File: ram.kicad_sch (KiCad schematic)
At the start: 20 parts, among them U19 7130, U7 74HCT245

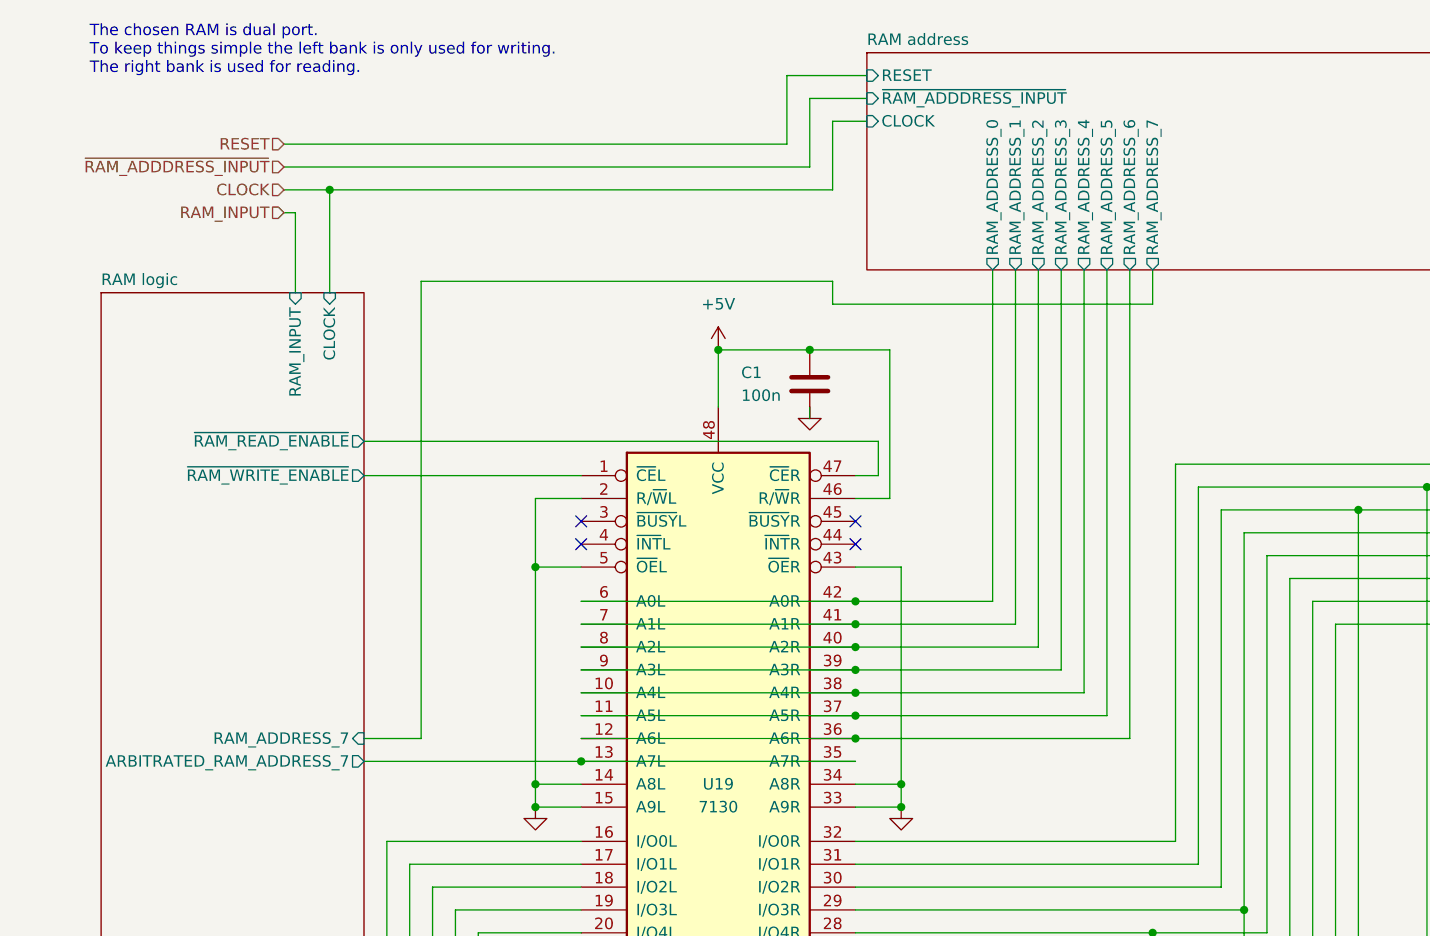
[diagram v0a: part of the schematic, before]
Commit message: ram address 7 led now uses the arbitrated signal
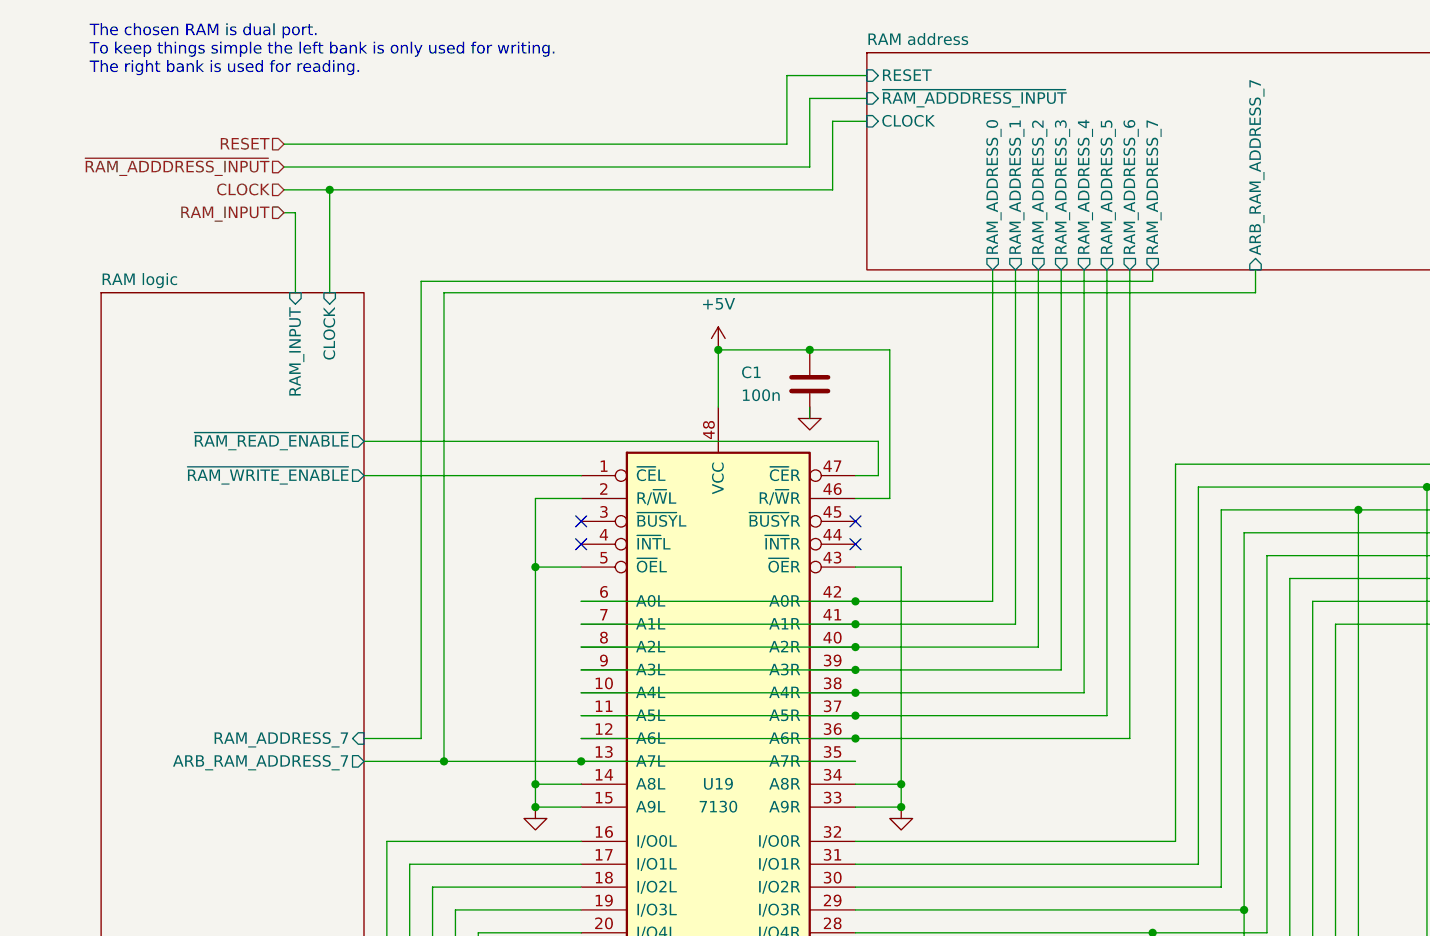
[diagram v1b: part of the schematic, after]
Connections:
- net RAM logic/ARBITRATED_RAM_ADDRESS_7 renamed RAM address/ARB_RAM_ADDRESS_7
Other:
- sheet RAM address ports: added ARB_RAM_ADDRESS_7; removed none
- sheet RAM logic ports: added ARB_RAM_ADDRESS_7; removed ARBITRATED_RAM_ADDRESS_7
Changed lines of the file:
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@@
   (junction (at 63.5 73.66) (diameter 0) (color 0 0 0 0)
+  )
+  (junction (at 53.34 95.25) (diameter 0) (color 0 0 0 0)
   )
   (junction (at 99.06 85.09) (diameter 0) (color 0 0 0 0)
@@
     (stroke (width 0) (type default))
   )
-  (wire (pts (xy 96.52 41.91) (xy 50.8 41.91))
+  (wire (pts (xy 50.8 41.91) (xy 132.08 41.91))
     (stroke (width 0) (type default))
   )
@@
     (stroke (width 0) (type default) (color 0 0 255 1))
   )
-  (wire (pts (xy 44.45 95.25) (xy 68.58 95.25))
-    (stroke (width 0) (type default))
-  )
-  (wire (pts (xy 132.08 44.45) (xy 96.52 44.45))
+  (wire (pts (xy 44.45 95.25) (xy 53.34 95.25))
     (stroke (width 0) (type default))
   )
@@
     (stroke (width 0) (type default))
   )
-  (wire (pts (xy 132.08 40.64) (xy 132.08 44.45))
+  (wire (pts (xy 132.08 40.64) (xy 132.08 41.91))
     (stroke (width 0) (type default))
   )
@@
     (stroke (width 0) (type default) (color 0 0 255 1))
   )
+  (wire (pts (xy 143.51 40.64) (xy 143.51 43.18))
+    (stroke (width 0) (type default))
+  )
   (wire (pts (xy 134.62 104.14) (xy 134.62 62.23))
     (stroke (width 0) (type default))
@@
     (stroke (width 0) (type default))
   )
+  (wire (pts (xy 53.34 95.25) (xy 68.58 95.25))
+    (stroke (width 0) (type default))
+  )
   (wire (pts (xy 99.06 119.38) (xy 111.76 119.38))
     (stroke (width 0) (type default))
@@
     (stroke (width 0) (type default) (color 255 0 0 1))
   )
+  (wire (pts (xy 143.51 43.18) (xy 53.34 43.18))
+    (stroke (width 0) (type default))
+  )
   (wire (pts (xy 256.54 31.75) (xy 256.54 74.93))
     (stroke (width 0) (type default) (color 0 0 255 1))
@@
     (stroke (width 0) (type default) (color 255 0 0 1))
   )
+  (wire (pts (xy 53.34 43.18) (xy 53.34 95.25))
+    (stroke (width 0) (type default))
+  )
   (wire (pts (xy 116.84 80.01) (xy 116.84 40.64))
     (stroke (width 0) (type default))
@@
   )
   (wire (pts (xy 147.32 116.84) (xy 121.92 116.84))
-    (stroke (width 0) (type default))
-  )
-  (wire (pts (xy 96.52 44.45) (xy 96.52 41.91))
     (stroke (width 0) (type default))
   )
@@
       (effects (font (size 1.27 1.27)) (justify left))
     )
+    (pin "ARB_RAM_ADDRESS_7" input (at 143.51 40.64 270)
+      (effects (font (size 1.27 1.27)) (justify left))
+    )
     (instances
       (project "8-bit-cpu"
@@
       (effects (font (size 1.27 1.27)) (justify left))
     )
-    (pin "ARBITRATED_RAM_ADDRESS_7" output (at 44.45 95.25 0)
-      (effects (font (size 1.27 1.27)) (justify right))
-    )
+    (pin "ARB_RAM_ADDRESS_7" output (at 44.45 95.25 0)
+      (effects (font (size 1.27 1.27)) (justify right))
+    )

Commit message: finished the control logic
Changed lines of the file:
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@@
     (effects (font (size 1.27 1.27)) (justify left))
   )
-  (hierarchical_label "~{RAM_OUTPUT}" (shape output) (at 269.24 100.33 0) (fields_autoplaced)
+  (hierarchical_label "~{RAM_OUTPUT}" (shape input) (at 269.24 100.33 0) (fields_autoplaced)
     (effects (font (size 1.27 1.27)) (justify left))
   )

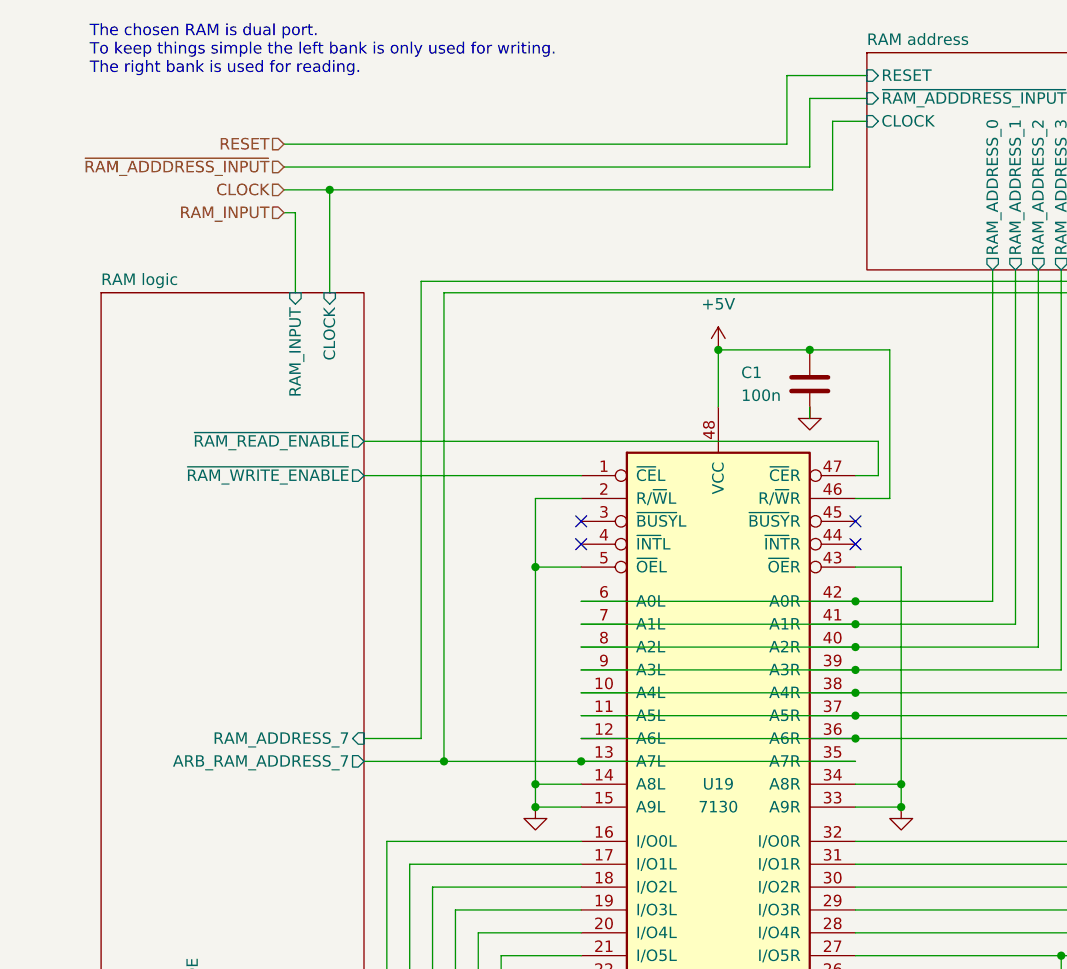
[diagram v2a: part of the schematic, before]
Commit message: added stack and x register.  Added logic for stack_address so ram address 7 gets passes and ram address 8 is high
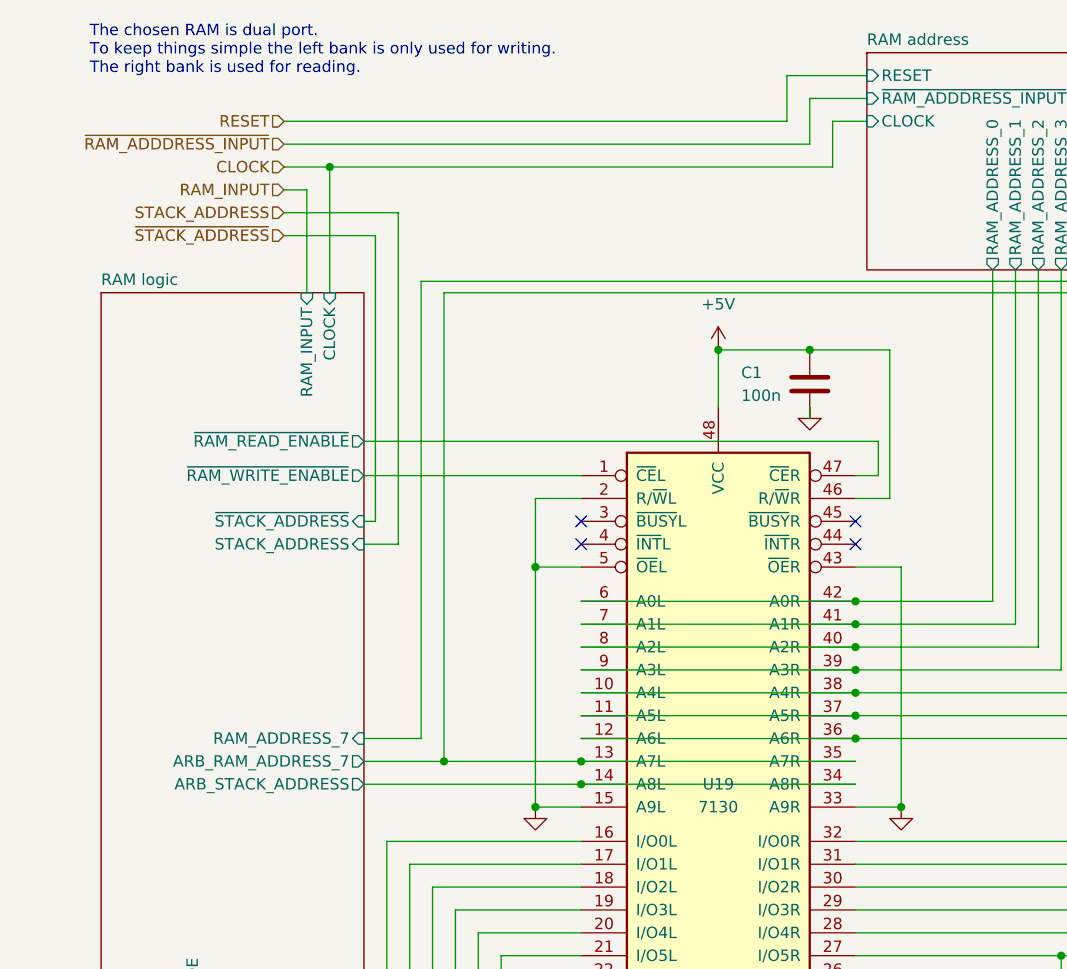
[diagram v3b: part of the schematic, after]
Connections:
- net GND: no longer U19.14 (A8L), U19.34 (A8R)
- new net RAM logic/ARB_STACK_ADDRESS: U19.14 (A8L), U19.34 (A8R)
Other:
- sheet RAM logic ports: added ARB_STACK_ADDRESS, STACK_ADDRESS, ~{STACK_ADDRESS}; removed none
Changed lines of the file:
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@@
   (junction (at 142.24 111.76) (diameter 0) (color 0 0 0 0)
   )
-  (junction (at 63.5 97.79) (diameter 0) (color 0 0 0 0)
-  )
   (junction (at 99.06 82.55) (diameter 0) (color 0 0 0 0)
   )
@@
   (junction (at 121.92 146.05) (diameter 0) (color 0 0 0 0)
   )
+  (junction (at 40.64 29.21) (diameter 0) (color 255 0 0 1)
+  )
   (junction (at 111.76 146.05) (diameter 0) (color 0 0 0 0)
   )
@@
   (junction (at 245.11 77.47) (diameter 0) (color 0 0 255 1)
   )
+  (junction (at 68.58 97.79) (diameter 0) (color 255 0 0 1)
+  )
   (junction (at 269.24 62.23) (diameter 0) (color 0 0 255 1)
   )
@@
   (junction (at 132.08 114.3) (diameter 0) (color 0 0 0 0)
   )
-  (junction (at 104.14 97.79) (diameter 0) (color 0 0 0 0)
-  )
   (junction (at 237.49 69.85) (diameter 0) (color 0 0 255 1)
   )
@@
   )
   (junction (at 142.24 146.05) (diameter 0) (color 0 0 0 0)
-  )
-  (junction (at 40.64 31.75) (diameter 0) (color 255 0 0 1)
   )
   (junction (at 132.08 146.05) (diameter 0) (color 0 0 0 0)
@@
     (stroke (width 0) (type default))
   )
-  (wire (pts (xy 91.44 26.67) (xy 35.56 26.67))
-    (stroke (width 0) (type default) (color 255 0 0 1))
-  )
-  (wire (pts (xy 99.06 97.79) (xy 104.14 97.79))
-    (stroke (width 0) (type default))
+  (wire (pts (xy 48.26 34.29) (xy 48.26 71.12))
+    (stroke (width 0) (type default) (color 255 0 0 1))
+  )
+  (wire (pts (xy 91.44 24.13) (xy 35.56 24.13))
+    (stroke (width 0) (type default) (color 255 0 0 1))
   )
   (wire (pts (xy 152.4 146.05) (xy 152.4 143.51))
     (stroke (width 0) (type default))
   )
-  (wire (pts (xy 93.98 29.21) (xy 35.56 29.21))
+  (wire (pts (xy 93.98 26.67) (xy 35.56 26.67))
     (stroke (width 0) (type default) (color 255 0 0 1))
   )
@@
     (stroke (width 0) (type default))
   )
+  (wire (pts (xy 35.56 36.83) (xy 45.72 36.83))
+    (stroke (width 0) (type default) (color 255 0 0 1))
+  )
   (wire (pts (xy 101.6 121.92) (xy 99.06 121.92))
     (stroke (width 0) (type default))
@@
     (stroke (width 0) (type default) (color 255 0 0 1))
   )
-  (wire (pts (xy 35.56 31.75) (xy 40.64 31.75))
+  (wire (pts (xy 35.56 29.21) (xy 40.64 29.21))
     (stroke (width 0) (type default) (color 255 0 0 1))
   )
@@
     (stroke (width 0) (type default) (color 0 0 255 1))
   )
-  (wire (pts (xy 36.83 34.29) (xy 36.83 43.18))
+  (wire (pts (xy 38.1 31.75) (xy 38.1 43.18))
     (stroke (width 0) (type default) (color 255 0 0 1))
   )
@@
     (stroke (width 0) (type default))
   )
-  (wire (pts (xy 104.14 73.66) (xy 104.14 97.79))
+  (wire (pts (xy 104.14 73.66) (xy 104.14 100.33))
     (stroke (width 0) (type default))
   )
@@
     (stroke (width 0) (type default))
   )
+  (wire (pts (xy 68.58 97.79) (xy 99.06 97.79))
+    (stroke (width 0) (type default) (color 255 0 0 1))
+  )
   (wire (pts (xy 198.12 29.21) (xy 259.08 29.21))
     (stroke (width 0) (type default) (color 0 0 255 1))
@@
     (stroke (width 0) (type default))
   )
-  (wire (pts (xy 104.14 97.79) (xy 104.14 100.33))
-    (stroke (width 0) (type default))
-  )
   (wire (pts (xy 149.86 119.38) (xy 149.86 77.47))
     (stroke (width 0) (type default))
@@
     (stroke (width 0) (type default))
   )
+  (wire (pts (xy 35.56 34.29) (xy 48.26 34.29))
+    (stroke (width 0) (type default) (color 255 0 0 1))
+  )
   (wire (pts (xy 68.58 92.71) (xy 99.06 92.71))
     (stroke (width 0) (type default))
@@
     (stroke (width 0) (type default))
   )
-  (wire (pts (xy 68.58 97.79) (xy 63.5 97.79))
-    (stroke (width 0) (type default))
-  )
   (wire (pts (xy 54.61 111.76) (xy 54.61 154.94))
     (stroke (width 0) (type default))
@@
     (stroke (width 0) (type default) (color 0 0 255 1))
   )
-  (wire (pts (xy 91.44 19.05) (xy 91.44 26.67))
+  (wire (pts (xy 91.44 19.05) (xy 91.44 24.13))
     (stroke (width 0) (type default) (color 255 0 0 1))
   )
@@
     (stroke (width 0) (type default))
   )
+  (wire (pts (xy 40.64 29.21) (xy 40.64 43.18))
+    (stroke (width 0) (type default) (color 255 0 0 1))
+  )
   (wire (pts (xy 59.69 116.84) (xy 59.69 154.94))
     (stroke (width 0) (type default))
@@
     (stroke (width 0) (type default))
   )
-  (wire (pts (xy 63.5 73.66) (xy 63.5 97.79))
+  (wire (pts (xy 63.5 73.66) (xy 63.5 100.33))
     (stroke (width 0) (type default))
   )
@@
     (stroke (width 0) (type default))
   )
+  (wire (pts (xy 48.26 71.12) (xy 44.45 71.12))
+    (stroke (width 0) (type default) (color 255 0 0 1))
+  )
   (wire (pts (xy 121.92 146.05) (xy 121.92 143.51))
     (stroke (width 0) (type default))
   )
+  (wire (pts (xy 44.45 97.79) (xy 68.58 97.79))
+    (stroke (width 0) (type default) (color 255 0 0 1))
+  )
   (wire (pts (xy 186.69 90.17) (xy 193.04 90.17))
     (stroke (width 0) (type default))
@@
     (stroke (width 0) (type default))
   )
-  (wire (pts (xy 63.5 97.79) (xy 63.5 100.33))
-    (stroke (width 0) (type default))
-  )
   (wire (pts (xy 220.98 67.31) (xy 234.95 67.31))
     (stroke (width 0) (type default) (color 0 0 255 1))
@@
     (stroke (width 0) (type default))
   )
-  (wire (pts (xy 93.98 21.59) (xy 93.98 29.21))
+  (wire (pts (xy 45.72 68.58) (xy 44.45 68.58))
+    (stroke (width 0) (type default) (color 255 0 0 1))
+  )
+  (wire (pts (xy 93.98 21.59) (xy 93.98 26.67))
     (stroke (width 0) (type default) (color 255 0 0 1))
   )
@@
     (stroke (width 0) (type default) (color 255 0 0 1))
   )
-  (wire (pts (xy 96.52 31.75) (xy 40.64 31.75))
+  (wire (pts (xy 96.52 29.21) (xy 40.64 29.21))
     (stroke (width 0) (type default) (color 255 0 0 1))
   )
@@
     (stroke (width 0) (type default) (color 0 0 255 1))
   )
+  (wire (pts (xy 45.72 36.83) (xy 45.72 68.58))
+    (stroke (width 0) (type default) (color 255 0 0 1))
+  )
   (wire (pts (xy 147.32 116.84) (xy 121.92 116.84))
     (stroke (width 0) (type default))
   )
-  (wire (pts (xy 96.52 24.13) (xy 96.52 31.75))
+  (wire (pts (xy 96.52 24.13) (xy 96.52 29.21))
     (stroke (width 0) (type default) (color 255 0 0 1))
   )
@@
     (stroke (width 0) (type default))
   )
-  (wire (pts (xy 40.64 31.75) (xy 40.64 43.18))
-    (stroke (width 0) (type default) (color 255 0 0 1))
-  )
   (wire (pts (xy 144.78 114.3) (xy 144.78 72.39))
     (stroke (width 0) (type default))
@@
     (stroke (width 0) (type default))
   )
-  (wire (pts (xy 35.56 34.29) (xy 36.83 34.29))
+  (wire (pts (xy 35.56 31.75) (xy 38.1 31.75))
     (stroke (width 0) (type default) (color 255 0 0 1))
   )
@@
     (effects (font (size 1.27 1.27)) (justify left))
   )
-  (hierarchical_label "RESET" (shape input) (at 35.56 26.67 180) (fields_autoplaced)
+  (hierarchical_label "RESET" (shape input) (at 35.56 24.13 180) (fields_autoplaced)
     (effects (font (size 1.27 1.27)) (justify right))
   )
@@
     (effects (font (size 1.27 1.27)) (justify left))
   )
+  (hierarchical_label "STACK_ADDRESS" (shape input) (at 35.56 34.29 180) (fields_autoplaced)
+    (effects (font (size 1.27 1.27)) (justify right))
+  )
   (hierarchical_label "BUS_4" (shape bidirectional) (at 270.51 72.39 0) (fields_autoplaced)
     (effects (font (size 1.27 1.27)) (justify left))
   )
+  (hierarchical_label "~{STACK_ADDRESS}" (shape input) (at 35.56 36.83 180) (fields_autoplaced)
+    (effects (font (size 1.27 1.27)) (justify right))
+  )
   (hierarchical_label "BUS_2" (shape bidirectional) (at 270.51 67.31 0) (fields_autoplaced)
     (effects (font (size 1.27 1.27)) (justify left))
@@
     (effects (font (size 1.27 1.27)) (justify left))
   )
-  (hierarchical_label "CLOCK" (shape input) (at 35.56 31.75 180) (fields_autoplaced)
+  (hierarchical_label "CLOCK" (shape input) (at 35.56 29.21 180) (fields_autoplaced)
     (effects (font (size 1.27 1.27)) (justify right))
   )
-  (hierarchical_label "RAM_INPUT" (shape input) (at 35.56 34.29 180) (fields_autoplaced)
+  (hierarchical_label "RAM_INPUT" (shape input) (at 35.56 31.75 180) (fields_autoplaced)
     (effects (font (size 1.27 1.27)) (justify right))
   )
-  (hierarchical_label "~{RAM_ADDDRESS_INPUT}" (shape input) (at 35.56 29.21 180) (fields_autoplaced)
+  (hierarchical_label "~{RAM_ADDDRESS_INPUT}" (shape input) (at 35.56 26.67 180) (fields_autoplaced)
     (effects (font (size 1.27 1.27)) (justify right))
   )
@@
       (effects (font (size 1.27 1.27)) (justify right))
     )
-    (pin "RAM_INPUT" input (at 36.83 43.18 90)
+    (pin "RAM_INPUT" input (at 38.1 43.18 90)
       (effects (font (size 1.27 1.27)) (justify right))
     )
@@
       (effects (font (size 1.27 1.27)) (justify right))
     )
+    (pin "STACK_ADDRESS" input (at 44.45 71.12 0)
+      (effects (font (size 1.27 1.27)) (justify right))
+    )
+    (pin "ARB_STACK_ADDRESS" output (at 44.45 97.79 0)
+      (effects (font (size 1.27 1.27)) (justify right))
+    )
+    (pin "~{STACK_ADDRESS}" input (at 44.45 68.58 0)
+      (effects (font (size 1.27 1.27)) (justify right))
+    )
